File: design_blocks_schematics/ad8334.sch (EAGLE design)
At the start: 66 parts, among them IC1 AD8334ACPZ

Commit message: further cleanup of todos
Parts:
- removed JP1, JP2: (no value), jumper:JP1E
- removed SLIDESWITCH1, SLIDESWITCH2: CL-SB-12A-01, wouter:CL-SB-12A-01
- added R10, R12: DNP, resistor:R-EU_R0603
- added R11, R2: 0R, resistor:R-EU_R0603
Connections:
- removed net 5V: L27.1, L28.1, L29.1, L30.1, L31.1, L32.1, R1.2, R3.2, SLIDESWITCH1.P$3, SLIDESWITCH2.P$3
- removed net N$10: GAIN12_1.CCW
- removed net N$7: JP1.2, R4.1
- removed net N$8: JP2.2, R5.1
- removed net N$9: GAIN34_1.CCW
- removed net VCM2: IC1.VCM2
- new net +5V: L27.1, L28.1, L29.1, L30.1, L31.1, L32.1, R1.2, R11.1, R2.1, R3.2
- new net N$3: IC1.COM1, IC1.COM2, IC1.GND_(EP), IC1.NC_5
- new net N$4: IC1.COM12, IC1.COM12_1, IC1.COM34_1, IC1.COM34_2
- new net VCM3: IC1.VCM4
- net CLAMP12_1: now also R4.1; no longer JP1.1
- net CLAMP12_2: now also R5.1; no longer JP2.1
- net GND: now also GAIN12_1.CCW, GAIN34_1.CCW, R10.2, R12.2; no longer IC1.COM1, IC1.COM12, IC1.COM12_1, IC1.COM2, IC1.COM34_1, IC1.COM34_2, IC1.GND_(EP), IC1.NC_5, SLIDESWITCH1.P$1, SLIDESWITCH2.P$1
- net HILO_12: now also R11.2, R12.1; no longer SLIDESWITCH2.P$2
- net MODE_12: now also R10.1, R2.2; no longer SLIDESWITCH1.P$2
- net R1_V1O_N: now also TP2_6.TP; no longer TP2_5.TP
- net R1_V1O_P: now also TP2_5.TP; no longer TP2_6.TP
- net R1_V2O_N: now also C6.1, IC1.VOL4
- net R1_V2O_P: now also C7.1, IC1.VOH4
- net R2_V2O_N: no longer C6.1, IC1.VOL4
- net R2_V2O_P: no longer C7.1, IC1.VOH4
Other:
- note added: "AD8334 - 2 Channels"
- note removed: "Channel 1,2"
- note removed: "TODO make ground symbols the same"
- note removed: "TODO: Power supplies"
- note removed: "todo: all vcm together?"
- note removed: "todo: attach to gnd or better solution? N$10 & N$9"
- note removed: "todo: can we reuse power supplies? todo: are names correct over multiple sheets?"
- note removed: "todo: change mode & hilo switches by resistor (easy to (de)solder)"
- moved on the sheet: C13, C14, C17, C18, C19, C20, C21, C22, C3, C4, C5, C51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

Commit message: further cleanup of todos
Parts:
- added R13, R14: 1K, resistor:R-EU_R0603
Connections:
- net +5V: now also R13.2, R14.2
- net EN12: now also R13.1
- net EN34: now also R14.1
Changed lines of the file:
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@@
 <part name="SUPPLY36" library="supply2" library_urn="urn:adsk.eagle:library:372" deviceset="GND" device=""/>
 <part name="SUPPLY37" library="supply2" library_urn="urn:adsk.eagle:library:372" deviceset="GND" device=""/>
+<part name="R13" library="resistor" library_urn="urn:adsk.eagle:library:348" deviceset="R-EU_" device="R0603" package3d_urn="urn:adsk.eagle:package:23555/3" value="1K"/>
+<part name="R14" library="resistor" library_urn="urn:adsk.eagle:library:348" deviceset="R-EU_" device="R0603" package3d_urn="urn:adsk.eagle:package:23555/3" value="1K"/>
+<part name="P+10" library="supply1" library_urn="urn:adsk.eagle:library:371" deviceset="+5V" device=""/>
+<part name="P+12" library="supply1" library_urn="urn:adsk.eagle:library:371" deviceset="+5V" device=""/>
 </parts>
 <sheets>
@@
 <attribute name="VALUE" x="269.875" y="197.485" size="1.778" layer="96"/>
 </instance>
+<instance part="R13" gate="G$1" x="208.28" y="182.88" smashed="yes" rot="R90">
+<attribute name="NAME" x="206.7814" y="179.07" size="1.778" layer="95" rot="R90"/>
+<attribute name="VALUE" x="211.582" y="179.07" size="1.778" layer="96" rot="R90"/>
+</instance>
+<instance part="R14" gate="G$1" x="215.9" y="182.88" smashed="yes" rot="R90">
+<attribute name="NAME" x="214.4014" y="179.07" size="1.778" layer="95" rot="R90"/>
+<attribute name="VALUE" x="219.202" y="179.07" size="1.778" layer="96" rot="R90"/>
+</instance>
+<instance part="P+10" gate="1" x="215.9" y="190.5" smashed="yes">
+<attribute name="VALUE" x="218.44" y="193.04" size="1.778" layer="96" rot="R180"/>
+</instance>
+<instance part="P+12" gate="1" x="208.28" y="190.5" smashed="yes">
+<attribute name="VALUE" x="210.82" y="193.04" size="1.778" layer="96" rot="R180"/>
+</instance>
 </instances>
 <busses>
@@
 <segment>
 <pinref part="IC1" gate="G$1" pin="HILO"/>
-<wire x1="213.36" y1="76.2" x2="213.367" y2="68.9458" width="0.1524" layer="91"/>
-<label x="213.24" y="61.502" size="1.778" layer="95" rot="R90"/>
+<wire x1="213.36" y1="76.2" x2="213.36" y2="60.96" width="0.1524" layer="91"/>
+<label x="213.36" y="60.96" size="1.778" layer="95" rot="R90"/>
 </segment>
 <segment>
@@
 <segment>
 <pinref part="IC1" gate="G$1" pin="EN12"/>
-<wire x1="215.9" y1="152.4" x2="215.9" y2="170.18" width="0.1524" layer="91"/>
+<wire x1="215.9" y1="152.4" x2="215.9" y2="172.72" width="0.1524" layer="91"/>
 <label x="215.9" y="154.94" size="1.778" layer="95" rot="R270" align="top-right"/>
+<pinref part="R13" gate="G$1" pin="1"/>
+<wire x1="208.28" y1="177.8" x2="208.28" y2="172.72" width="0.1524" layer="91"/>
+<wire x1="208.28" y1="172.72" x2="215.9" y2="172.72" width="0.1524" layer="91"/>
 </segment>
 </net>
@@
 <segment>
 <pinref part="IC1" gate="G$1" pin="EN34"/>
-<wire x1="218.44" y1="152.4" x2="218.44" y2="170.18" width="0.1524" layer="91"/>
+<wire x1="218.44" y1="152.4" x2="218.44" y2="175.26" width="0.1524" layer="91"/>
 <label x="218.44" y="154.94" size="1.778" layer="95" rot="R270" align="top-right"/>
+<wire x1="218.44" y1="175.26" x2="215.9" y2="175.26" width="0.1524" layer="91"/>
+<pinref part="R14" gate="G$1" pin="1"/>
+<wire x1="215.9" y1="175.26" x2="215.9" y2="177.8" width="0.1524" layer="91"/>
 </segment>
 </net>
@@
 <segment>
 <pinref part="IC1" gate="G$1" pin="GAIN34"/>
-<wire x1="208.28" y1="76.2" x2="208.2508" y2="65.922" width="0.1524" layer="91"/>
+<wire x1="208.28" y1="76.2" x2="208.2508" y2="60.842" width="0.1524" layer="91"/>
 <label x="208.2" y="60.942" size="1.778" layer="95" rot="R90"/>
 </segment>
@@
 <segment>
 <pinref part="IC1" gate="G$1" pin="CLMP34"/>
-<wire x1="210.82" y1="76.2" x2="210.7654" y2="65.122" width="0.1524" layer="91"/>
-<label x="210.74" y="60.142" size="1.778" layer="95" rot="R90"/>
+<wire x1="210.82" y1="76.2" x2="210.82" y2="60.96" width="0.1524" layer="91"/>
+<label x="210.82" y="60.96" size="1.778" layer="95" rot="R90"/>
 </segment>
 </net>
@@
 <segment>
 <pinref part="IC1" gate="G$1" pin="VPS4"/>
-<wire x1="205.74" y1="76.2" x2="205.74" y2="68.072" width="0.1524" layer="91"/>
-<label x="205.74" y="60.706" size="1.778" layer="95" rot="R90"/>
+<wire x1="205.74" y1="76.2" x2="205.74" y2="60.96" width="0.1524" layer="91"/>
+<label x="205.74" y="60.96" size="1.778" layer="95" rot="R90"/>
 </segment>
 <segment>
@@
 <pinref part="R11" gate="G$1" pin="1"/>
 </segment>
-</net>
+<segment>
+<pinref part="P+10" gate="1" pin="+5V"/>
+<pinref part="R14" gate="G$1" pin="2"/>
+</segment>
+<segment>
+<pinref part="P+12" gate="1" pin="+5V"/>
+<pinref part="R13" gate="G$1" pin="2"/>
+</segment>
+</net>

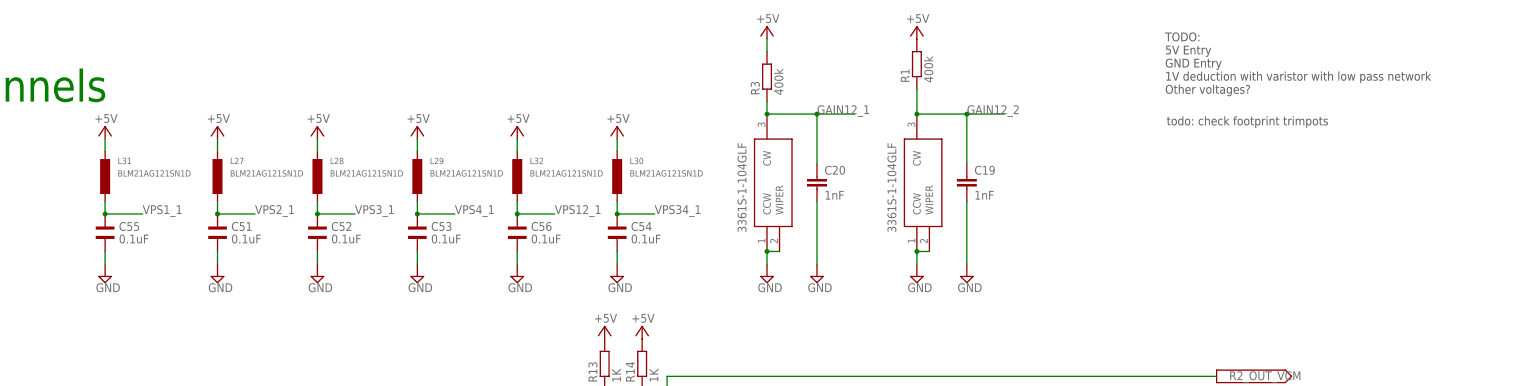
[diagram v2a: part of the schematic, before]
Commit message: finalized schematic
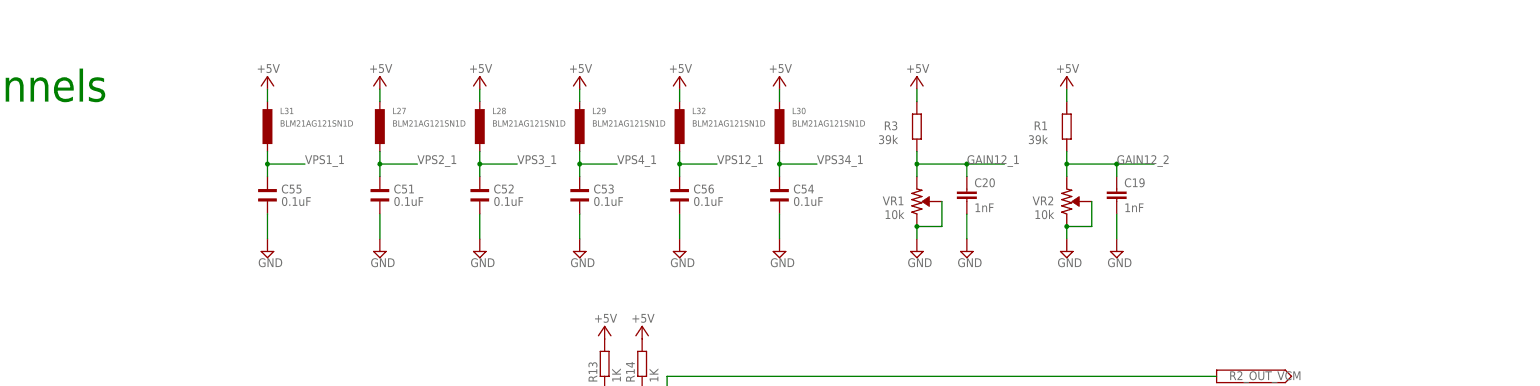
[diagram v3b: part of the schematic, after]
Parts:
- removed GAIN12_1, GAIN34_1: 3361S-1-104GLF, 3361S-1-104GLF:3361S-1-104GLF
- added VR1, VR2: 10k, SparkFun-Resistors:TRIMPOT-SMD-3MM-OPEN-1/10W-25%
- R1, R3: value 400k -> 39k
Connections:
- net GAIN12_1: now also VR1.CCW; no longer GAIN12_1.CW
- net GAIN12_2: now also VR2.CCW; no longer GAIN34_1.CW
- net GND: now also VR1.CW, VR1.WIPER, VR2.CW, VR2.WIPER; no longer GAIN12_1.CCW, GAIN12_1.WIPER, GAIN34_1.CCW, GAIN34_1.WIPER
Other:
- note removed: "TODO: 5V Entry GND Entry 1V deduction with varistor with low pass network Other voltages?"
- note removed: "todo: check footprint trimpots"
- moved on the sheet: C19, C20, C51, C52, C53, C54, C55, C56, L27, L28, L29, L30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

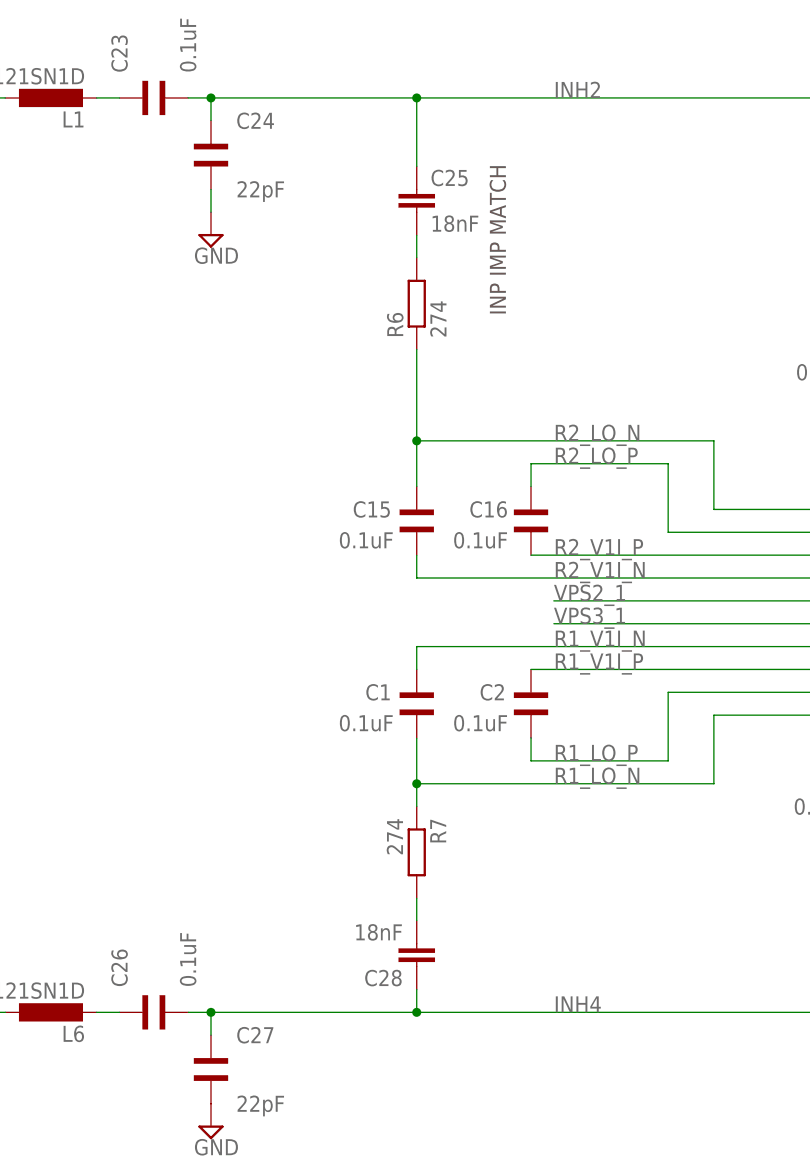
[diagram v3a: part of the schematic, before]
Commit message: routed input section
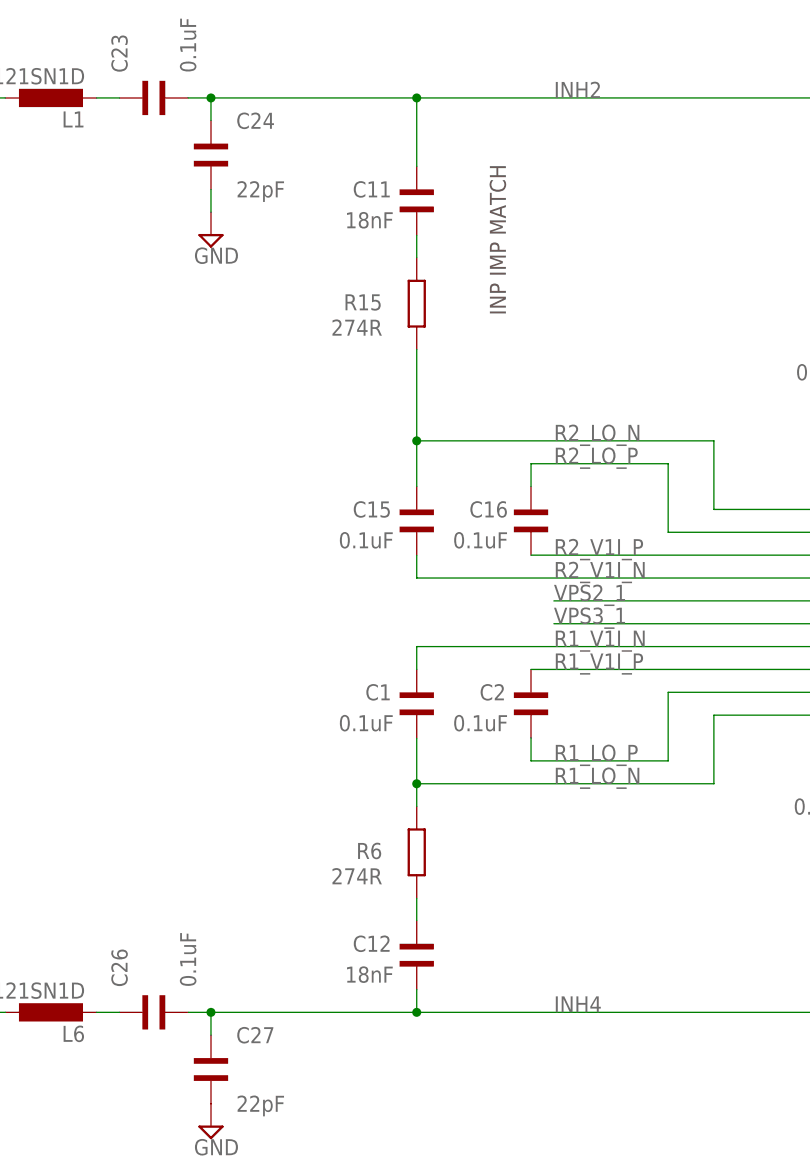
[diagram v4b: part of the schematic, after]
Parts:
- removed C25, C28: 18nF, rcl:C-EUC0603
- removed R7: 274, resistor:R-EU_R0603
- added C11, C12: 18nF, Wurth_Elektronik_Passive_Capacitors_rev18b:WCAP-CSGP_0402_885012205037
- added R15: 274R, resistor:R-EU_R0402
- R6: value 274 -> 274R; device resistor:R-EU_R0603 -> resistor:R-EU_R0402
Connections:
- net INH2: now also C11.2; no longer C25.1
- net INH4: now also C12.1; no longer C28.1
- net N$12: now also C11.1, R15.2; no longer C25.2, R6.2
- net N$14: now also C12.2, R6.1; no longer C28.2, R7.2
- net R1_LO_N: now also R6.2; no longer R7.1
- net R2_LO_N: now also R15.1; no longer R6.1
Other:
- moved on the sheet: R6
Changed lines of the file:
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@@
 <part name="C24" library="Wurth_Elektronik_Passive_Capacitors_rev18b" library_urn="urn:adsk.eagle:library:491551" deviceset="WCAP-CSGP_0402" device="" package3d_urn="urn:adsk.eagle:package:491821/2" technology="_885012005009" value="22pF"/>
 <part name="SUPPLY13" library="supply2" library_urn="urn:adsk.eagle:library:372" deviceset="GND" device=""/>
-<part name="C25" library="rcl" library_urn="urn:adsk.eagle:library:334" deviceset="C-EU" device="C0603" package3d_urn="urn:adsk.eagle:package:23616/2" value="18nF"/>
-<part name="R6" library="resistor" library_urn="urn:adsk.eagle:library:348" deviceset="R-EU_" device="R0603" package3d_urn="urn:adsk.eagle:package:23555/3" value="274"/>
 <part name="C26" library="Wurth_Elektronik_Passive_Capacitors_rev18b" library_urn="urn:adsk.eagle:library:491551" deviceset="WCAP-CSGP_0402" device="" package3d_urn="urn:adsk.eagle:package:491821/2" technology="_885012205037" value="0.1uF"/>
 <part name="C27" library="Wurth_Elektronik_Passive_Capacitors_rev18b" library_urn="urn:adsk.eagle:library:491551" deviceset="WCAP-CSGP_0402" device="" package3d_urn="urn:adsk.eagle:package:491821/2" technology="_885012005009" value="22pF"/>
-<part name="C28" library="rcl" library_urn="urn:adsk.eagle:library:334" deviceset="C-EU" device="C0603" package3d_urn="urn:adsk.eagle:package:23616/2" value="18nF"/>
-<part name="R7" library="resistor" library_urn="urn:adsk.eagle:library:348" deviceset="R-EU_" device="R0603" package3d_urn="urn:adsk.eagle:package:23555/3" value="274"/>
 <part name="D1" library="BAT64-04E6433" deviceset="BAT64-04E6433" device=""/>
 <part name="D2" library="BAT64-04E6433" deviceset="BAT64-04E6433" device=""/>
@@
 <part name="VR1" library="SparkFun-Resistors" library_urn="urn:adsk.eagle:library:532" deviceset="TRIMPOT" device="-SMD-3MM-OPEN-1/10W-25%" package3d_urn="urn:adsk.eagle:package:39666/1" value="10k"/>
 <part name="VR2" library="SparkFun-Resistors" library_urn="urn:adsk.eagle:library:532" deviceset="TRIMPOT" device="-SMD-3MM-OPEN-1/10W-25%" package3d_urn="urn:adsk.eagle:package:39666/1" value="10k"/>
+<part name="C11" library="Wurth_Elektronik_Passive_Capacitors_rev18b" library_urn="urn:adsk.eagle:library:491551" deviceset="WCAP-CSGP_0402" device="" package3d_urn="urn:adsk.eagle:package:491821/2" technology="_885012205037" value="18nF"/>
+<part name="C12" library="Wurth_Elektronik_Passive_Capacitors_rev18b" library_urn="urn:adsk.eagle:library:491551" deviceset="WCAP-CSGP_0402" device="" package3d_urn="urn:adsk.eagle:package:491821/2" technology="_885012205037" value="18nF"/>
+<part name="R15" library="resistor" library_urn="urn:adsk.eagle:library:348" deviceset="R-EU_" device="R0402" package3d_urn="urn:adsk.eagle:package:26058/2" value="274R"/>
+<part name="R6" library="resistor" library_urn="urn:adsk.eagle:library:348" deviceset="R-EU_" device="R0402" package3d_urn="urn:adsk.eagle:package:26058/2" value="274R"/>
 </parts>
 <sheets>
@@
 <attribute name="VALUE" x="74.295" y="151.765" size="1.778" layer="96"/>
 </instance>
-<instance part="C25" gate="G$1" x="99.06" y="160.02" smashed="yes">
-<attribute name="NAME" x="100.584" y="160.401" size="1.778" layer="95"/>
-<attribute name="VALUE" x="100.584" y="155.321" size="1.778" layer="96"/>
-</instance>
-<instance part="R6" gate="G$1" x="99.06" y="147.32" smashed="yes" rot="R90">
-<attribute name="NAME" x="97.5614" y="143.51" size="1.778" layer="95" rot="R90"/>
-<attribute name="VALUE" x="102.362" y="143.51" size="1.778" layer="96" rot="R90"/>
-</instance>
 <instance part="C26" gate="G$1" x="71.12" y="68.58" smashed="yes" rot="R90">
 <attribute name="NAME" x="66.929" y="71.374" size="1.778" layer="95" rot="R90"/>
@@
 <attribute name="NAME" x="78.994" y="65.151" size="1.778" layer="95"/>
 <attribute name="VALUE" x="78.994" y="57.531" size="1.778" layer="96"/>
-</instance>
-<instance part="C28" gate="G$1" x="99.06" y="73.66" smashed="yes" rot="R180">
-<attribute name="NAME" x="97.536" y="73.279" size="1.778" layer="95" rot="R180"/>
-<attribute name="VALUE" x="97.536" y="78.359" size="1.778" layer="96" rot="R180"/>
-</instance>
-<instance part="R7" gate="G$1" x="99.06" y="86.36" smashed="yes" rot="R270">
-<attribute name="NAME" x="100.5586" y="90.17" size="1.778" layer="95" rot="R270"/>
-<attribute name="VALUE" x="95.758" y="90.17" size="1.778" layer="96" rot="R270"/>
 </instance>
 <instance part="D1" gate="G$1" x="43.18" y="127" smashed="yes" rot="R90">
@@
 <attribute name="NAME" x="299.72" y="216.916" size="1.778" layer="95" font="vector" rot="R180"/>
 <attribute name="VALUE" x="299.72" y="212.344" size="1.778" layer="96" font="vector" rot="R180" align="top-left"/>
+</instance>
+<instance part="C11" gate="G$1" x="99.06" y="157.48" smashed="yes">
+<attribute name="NAME" x="96.266" y="160.909" size="1.778" layer="95" rot="R180"/>
+<attribute name="VALUE" x="96.52" y="157.48" size="1.778" layer="96" rot="R180"/>
+</instance>
+<instance part="C12" gate="G$1" x="99.06" y="73.66" smashed="yes">
+<attribute name="NAME" x="96.266" y="77.089" size="1.778" layer="95" rot="R180"/>
+<attribute name="VALUE" x="96.52" y="73.66" size="1.778" layer="96" rot="R180"/>
+</instance>
+<instance part="R15" gate="G$1" x="99.06" y="147.32" smashed="yes" rot="R90">
+<attribute name="NAME" x="95.25" y="148.3614" size="1.778" layer="95" rot="R180"/>
+<attribute name="VALUE" x="95.25" y="145.542" size="1.778" layer="96" rot="R180"/>
+</instance>
+<instance part="R6" gate="G$1" x="99.06" y="86.36" smashed="yes" rot="R90">
+<attribute name="NAME" x="95.25" y="87.4014" size="1.778" layer="95" rot="R180"/>
+<attribute name="VALUE" x="95.25" y="84.582" size="1.778" layer="96" rot="R180"/>
 </instance>
 </instances>
@@
 <pinref part="C1" gate="G$1" pin="1"/>
 <wire x1="99.06" y1="93.98" x2="99.06" y2="99.06" width="0.1524" layer="91"/>
-<pinref part="R7" gate="G$1" pin="1"/>
 <wire x1="99.06" y1="91.44" x2="99.06" y2="93.98" width="0.1524" layer="91"/>
 <junction x="99.06" y="93.98"/>
 <label x="114.3" y="93.98" size="1.778" layer="95"/>
+<pinref part="R6" gate="G$1" pin="2"/>
 </segment>
 </net>
@@
 <label x="114.3" y="132.08" size="1.778" layer="95"/>
 <wire x1="99.06" y1="127" x2="99.06" y2="132.08" width="0.1524" layer="91"/>
-<pinref part="R6" gate="G$1" pin="1"/>
 <wire x1="99.06" y1="142.24" x2="99.06" y2="132.08" width="0.1524" layer="91"/>
 <junction x="99.06" y="132.08"/>
@@
 <wire x1="132.08" y1="132.08" x2="132.08" y2="124.46" width="0.1524" layer="91"/>
 <wire x1="132.08" y1="124.46" x2="175.26" y2="124.46" width="0.1524" layer="91"/>
+<pinref part="R15" gate="G$1" pin="1"/>
 </segment>
 </net>
@@
 <wire x1="99.06" y1="170.18" x2="76.2" y2="170.18" width="0.1524" layer="91"/>
 <wire x1="165.1" y1="132.08" x2="165.1" y2="170.18" width="0.1524" layer="91"/>
-<pinref part="C25" gate="G$1" pin="1"/>
 <wire x1="99.06" y1="162.56" x2="99.06" y2="170.18" width="0.1524" layer="91"/>
 <junction x="99.06" y="170.18"/>
+<pinref part="C11" gate="G$1" pin="2"/>
 </segment>
 </net>
 <net name="N$12" class="0">
 <segment>
-<pinref part="C25" gate="G$1" pin="2"/>
-<pinref part="R6" gate="G$1" pin="2"/>
 <wire x1="99.06" y1="152.4" x2="99.06" y2="154.94" width="0.1524" layer="91"/>
+<pinref part="C11" gate="G$1" pin="1"/>
+<pinref part="R15" gate="G$1" pin="2"/>
 </segment>
 </net>
@@
 <net name="N$14" class="0">
 <segment>
-<pinref part="C28" gate="G$1" pin="2"/>
-<pinref part="R7" gate="G$1" pin="2"/>
 <wire x1="99.06" y1="81.28" x2="99.06" y2="78.74" width="0.1524" layer="91"/>
+<pinref part="C12" gate="G$1" pin="2"/>
+<pinref part="R6" gate="G$1" pin="1"/>
 </segment>
 </net>
@@
 <label x="114.3" y="68.58" size="1.778" layer="95"/>
 <pinref part="C27" gate="G$1" pin="2"/>
-<pinref part="C28" gate="G$1" pin="1"/>
 <pinref part="IC1" gate="G$1" pin="INH3"/>
 <wire x1="175.26" y1="93.98" x2="165.1" y2="93.98" width="0.1524" layer="91"/>
@@
 <wire x1="99.06" y1="68.58" x2="165.1" y2="68.58" width="0.1524" layer="91"/>
 <junction x="99.06" y="68.58"/>
-</segment>
-</net>
-<net name="LVOUT_1" class="0">
+<pinref part="C12" gate="G$1" pin="1"/>
+</segment>
+</net>
+<net name="LVOUT_1" class="2">
 <segment>
 <label x="25.4" y="68.58" size="1.778" layer="95" rot="R180" align="top-right"/>
